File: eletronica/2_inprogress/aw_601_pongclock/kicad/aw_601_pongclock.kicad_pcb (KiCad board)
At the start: 2 copper layers, 149.9 x 199.4 mm, 89 parts, among them IC1 ATMEGA8-P, Q1 2N3904G, Q10 2N3904G, Q11 2N3904G, Q12 2N3904G, Q13 2N3904G, Q14 2N3904G, Q15 2N3904G, Q16 2N3904G, Q17 2N3904G, Q18 2N3904G, Q19 2N3904G, Q2 2N3904G, Q20 2N3904G, Q21 2N3904G, Q22 2N3904G, Q23 2N3904G, Q24 2N3904G, Q25 2N3904G, Q26 2N3904G, Q27 2N3904G, Q28 2N3904G, Q29 2N3904G, Q3 2N3904G, Q30 2N3904G, Q31 2N3904G, Q32 2N3904G, Q4 2N3904G, Q5 2N3904G, Q6 2N3904G, Q7 2N3904G, Q8 2N3904G, Q9 2N3904G, SW1 SW_PUSH, SW2 SW_PUSH, SW3 SW_PUSH, SW4 SW_PUSH, U1 4514, U2 ULN2803, U3 ULN2803, U4 ULN2803, U5 ULN2803, U6 74HC4094, U7 74HC4094, U8 74HC4094, U9 74HC4094, X1 16Mhz

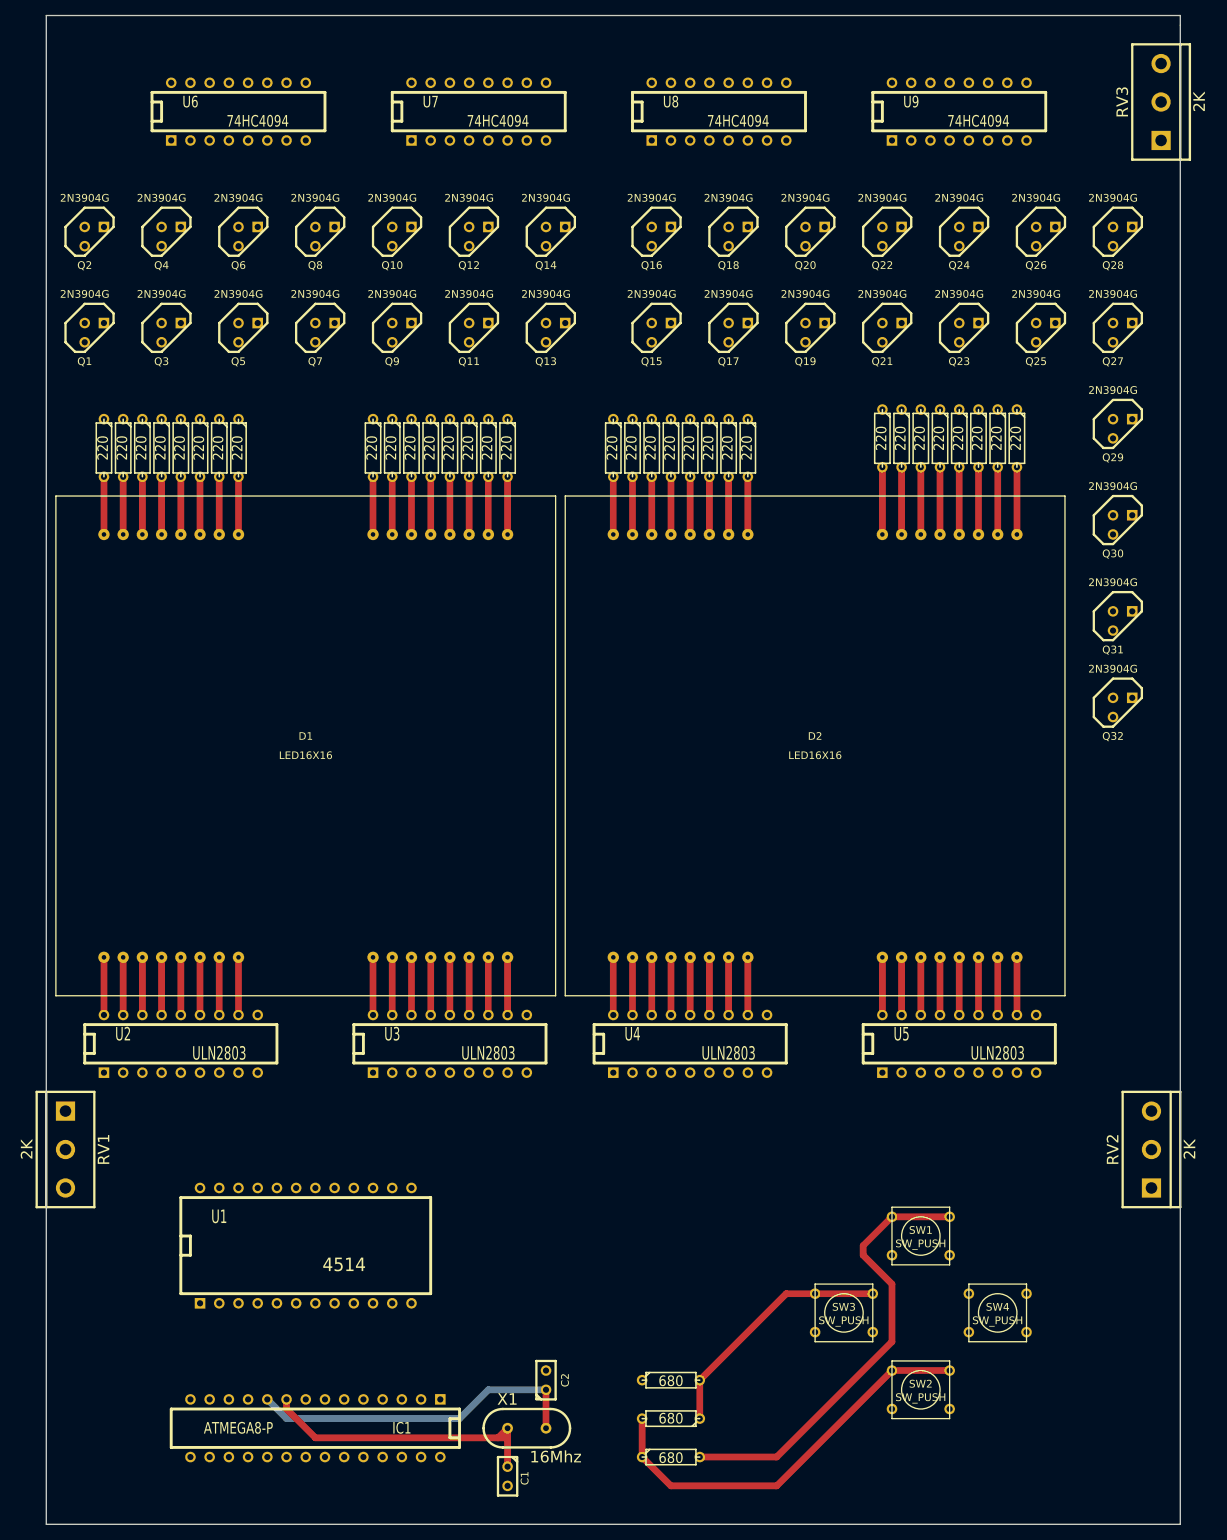
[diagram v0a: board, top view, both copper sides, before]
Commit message: 
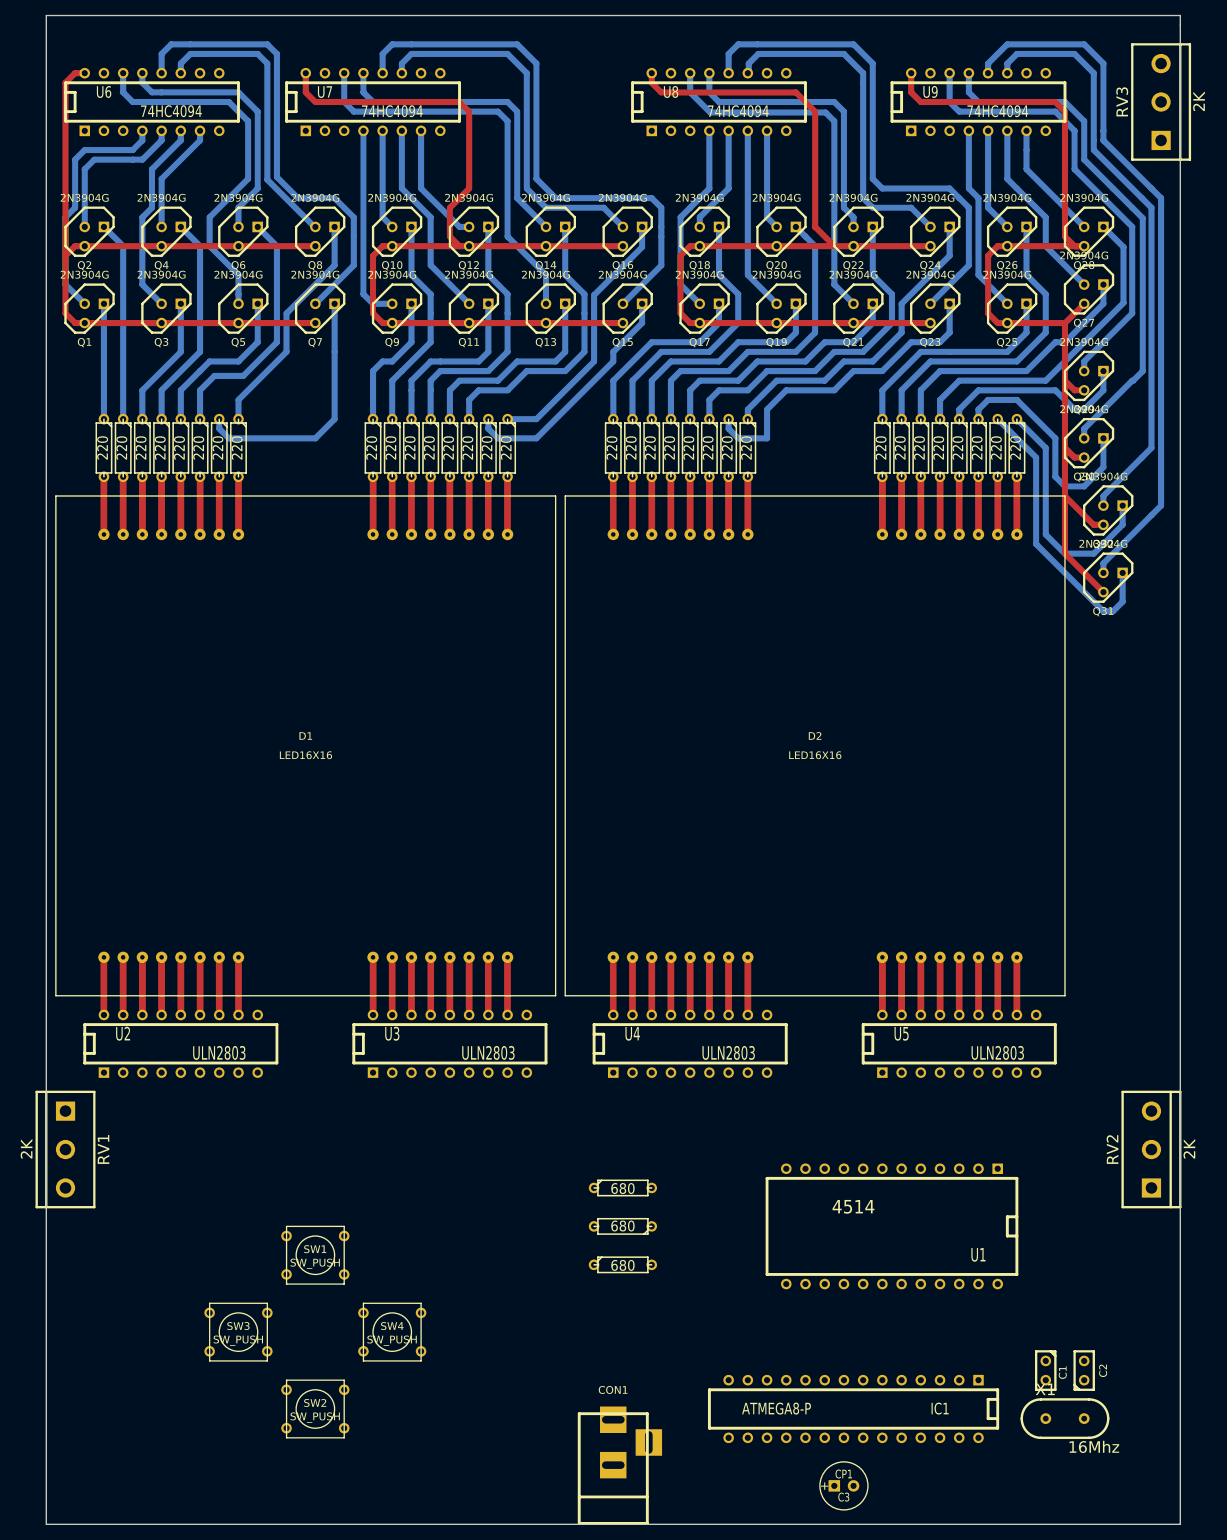
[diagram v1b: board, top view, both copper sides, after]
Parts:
- added C3: CP1, C1V7, F.Cu at (141.0, 232.4)
- added CON1: BARREL_JACK, BARREL_JACK, F.Cu at (110.5, 229.9)
- moved SW1 80.1 mm to (71.1, 201.9)
- moved SW2 80.1 mm to (71.1, 222.2)
- moved SW3 80.1 mm to (61.0, 212.1)
- moved SW4 80.1 mm to (81.3, 212.1)
- moved U1 77.5 mm to (147.3, 198.1), turned to 180 degrees
- moved C1 72.5 mm to (167.6, 217.2)
- moved IC1 71.2 mm to (142.2, 222.2)
- moved C2 71.1 mm to (172.7, 217.2)
- moved X1 71.1 mm to (170.2, 223.5)
- moved R1 26.2 mm to (111.8, 203.2)
- moved R2 26.2 mm to (111.8, 198.1)
- moved R3 26.2 mm to (111.8, 193.0)
- moved Q32 25.4 mm to (176.5, 104.1)
- moved U7 14.0 mm to (78.7, 49.5)
- moved U6 11.5 mm to (49.5, 49.5)
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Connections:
- Q1 pad 1: (no net) -> N-000008
- Q1 pad 2: N-0000027 -> /V1
- Q10 pad 1: (no net) -> N-000004
- Q10 pad 2: N-0000045 (its old number) -> /V10
- Q11 pad 1: (no net) -> N-000005
- Q11 pad 2: N-0000049 -> /V11
- Q12 pad 1: (no net) -> N-000006
- Q12 pad 2: N-0000050 -> /V12
- Q13 pad 1: (no net) -> N-0000019
- Q14 pad 1: (no net) -> N-0000020
- Q15 pad 1: (no net) -> N-0000021
- Q16 pad 1: (no net) -> N-0000022
- Q17 pad 1: (no net) -> N-0000016
- Q18 pad 1: (no net) -> N-0000015
- Q19 pad 1: (no net) -> N-0000014
- Q2 pad 1: (no net) -> N-0000012
- Q2 pad 2: N-0000054 -> /V2
- Q20 pad 1: (no net) -> N-0000013
- Q21 pad 1: (no net) -> N-0000024
- Q22 pad 1: (no net) -> N-0000023
- Q23 pad 1: (no net) -> N-0000017
- Q24 pad 1: (no net) -> N-0000018
- Q25 pad 1: (no net) -> N-0000064
- Q26 pad 1: (no net) -> N-0000065
- Q27 pad 1: (no net) -> N-0000066
- Q28 pad 1: (no net) -> N-0000067
- Q29 pad 1: (no net) -> N-0000068
- Q3 pad 1: (no net) -> N-000007
- Q3 pad 2: N-0000053 -> /V3
- Q30 pad 1: (no net) -> N-0000060
- Q31 pad 1: (no net) -> N-0000061
- Q32 pad 1: (no net) -> N-0000062
- Q4 pad 1: (no net) -> N-0000011
- Q4 pad 2: N-0000052 -> /V4
- Q5 pad 1: (no net) -> N-0000010
- Q5 pad 2: N-0000051 -> /V5
- Q6 pad 1: (no net) -> N-000009
- Q7 pad 1: (no net) -> N-000001
- Q7 pad 2: N-0000046 (its old number) -> /V7
- Q8 pad 1: (no net) -> N-000002
- Q8 pad 2: N-0000047 -> /V8
- Q9 pad 1: (no net) -> N-000003
- Q9 pad 2: N-0000048 -> /V9
- R10 pad 1: N-0000046 (its old number) -> N-000001
- R27 pad 1: N-0000047 -> N-000002
- R28 pad 1: N-0000048 -> N-000003
- R29 pad 1: N-0000045 (its old number) -> N-000004
- R30 pad 1: N-0000049 -> N-000005
- R31 pad 1: N-0000050 -> N-000006
- R32 pad 1: (no net) -> N-0000019
- R33 pad 1: (no net) -> N-0000020
- R34 pad 1: (no net) -> N-0000021
- R35 pad 1: (no net) -> N-0000022
- R4 pad 1: N-0000027 -> N-000008
- R5 pad 1: N-0000054 -> N-0000012
- R52 pad 1: (no net) -> N-0000016
- R53 pad 1: (no net) -> N-0000015
- R54 pad 1: (no net) -> N-0000014
- R55 pad 1: (no net) -> N-0000013
- R56 pad 1: (no net) -> N-0000024
- R57 pad 1: (no net) -> N-0000023
- R58 pad 1: (no net) -> N-0000017
- R59 pad 1: (no net) -> N-0000018
- R6 pad 1: N-0000053 -> N-000007
- R60 pad 1: (no net) -> N-0000064
- R61 pad 1: (no net) -> N-0000065
- R62 pad 1: (no net) -> N-0000066
- R63 pad 1: (no net) -> N-0000067
- R64 pad 1: (no net) -> N-0000068
- R65 pad 1: (no net) -> N-0000060
- R66 pad 1: (no net) -> N-0000061
- R67 pad 1: (no net) -> N-0000062
- R7 pad 1: N-0000052 -> N-0000011
- R8 pad 1: N-0000051 -> N-0000010
- R9 pad 1: (no net) -> N-000009
- U6 pad 11: (no net) -> /V8
- U6 pad 12: (no net) -> /V7
- U6 pad 14: (no net) -> /V5
- U6 pad 4: (no net) -> /V1
- U6 pad 5: (no net) -> /V2
- U6 pad 6: (no net) -> /V3
- U6 pad 7: (no net) -> /V4
- U7 pad 4: (no net) -> /V9
- U7 pad 5: (no net) -> /V10
- U7 pad 6: (no net) -> /V11
- U7 pad 7: (no net) -> /V12
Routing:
- net +5V: track 0.00 -> 466.9 mm
- net /V31: track 0.00 -> 92.2 mm
- net /V32: track 0.00 -> 77.2 mm
- net /V15: track 0.00 -> 72.6 mm
- net /V30: track 0.00 -> 67.8 mm
- net /V23: track 0.00 -> 67.5 mm
- net /V7: track 0.00 -> 61.0 mm
- net /V29: track 0.00 -> 59.4 mm
- net N-00000105: track 59.0 -> 0.00 mm
- net N-00000103: track 53.6 -> 0.00 mm
- net /V13: track 0.00 -> 52.7 mm
- net /V16: track 0.00 -> 49.4 mm
- net /V5: track 0.00 -> 48.4 mm
- net /V21: track 0.00 -> 48.4 mm
- net /V24: track 0.00 -> 45.0 mm
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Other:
- net class Default: clearance 0.5 -> 0.35; trace_width 0.889 -> 0.8
- rule trace_clearance: 0.5 -> 0.35

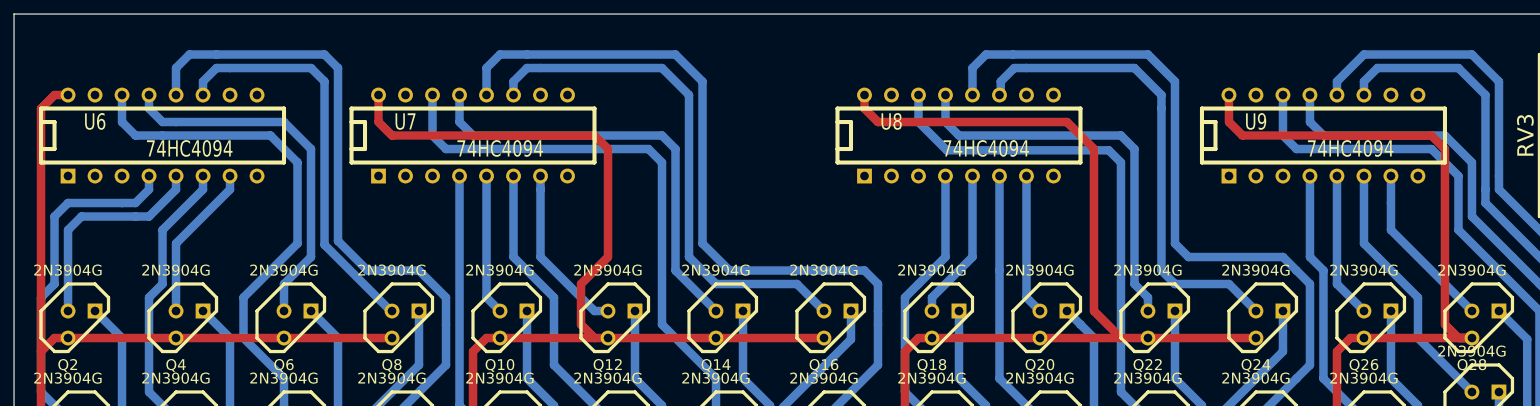
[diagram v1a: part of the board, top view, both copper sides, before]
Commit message: 
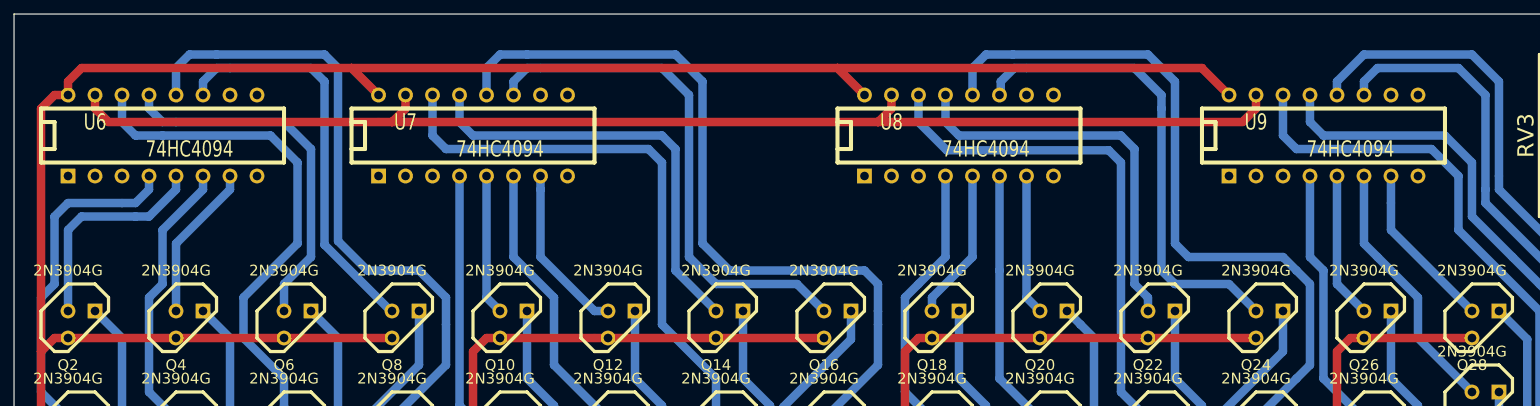
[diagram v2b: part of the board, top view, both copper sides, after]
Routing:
- net /OE: track 0.00 -> 118.9 mm
- net +5V: track 466.9 -> 454.9 mm
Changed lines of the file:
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@@
   (general
     (links 273)
-    (no_connects 113)
+    (no_connects 110)
     (area 31.7556 38.049999 189.2244 237.911121)
     (thickness 1.6)
     (drawings 5)
-    (tracks 588)
+    (tracks 587)
     (zones 0)
     (modules 91)
@@
   (gr_line (start 35.56 237.49) (end 185.42 237.49) (angle 90) (layer Edge.Cuts) (width 0.1))
   (gr_line (start 35.56 38.1) (end 35.56 237.49) (angle 90) (layer Edge.Cuts) (width 0.1))
-  (segment (start 149.86 45.72) (end 149.86 48.26) (width 0.8) (layer F.Cu) (net 1) (status 400000))
-  (segment (start 171.45 68.58) (end 172.72 68.58) (width 0.8) (layer F.Cu) (net 1) (status 800000))
-  (segment (start 170.18 67.31) (end 171.45 68.58) (width 0.8) (layer F.Cu) (net 1))
-  (segment (start 170.18 50.8) (end 170.18 67.31) (width 0.8) (layer F.Cu) (net 1))
-  (segment (start 168.91 49.53) (end 170.18 50.8) (width 0.8) (layer F.Cu) (net 1))
-  (segment (start 151.13 49.53) (end 168.91 49.53) (width 0.8) (layer F.Cu) (net 1))
-  (segment (start 149.86 48.26) (end 151.13 49.53) (width 0.8) (layer F.Cu) (net 1))
-  (segment (start 115.57 45.72) (end 115.57 46.99) (width 0.8) (layer F.Cu) (net 1) (status 400000))
-  (segment (start 137.16 66.04) (end 139.7 68.58) (width 0.8) (layer F.Cu) (net 1))
-  (segment (start 137.16 50.8) (end 137.16 66.04) (width 0.8) (layer F.Cu) (net 1))
-  (segment (start 134.62 48.26) (end 137.16 50.8) (width 0.8) (layer F.Cu) (net 1))
-  (segment (start 116.84 48.26) (end 134.62 48.26) (width 0.8) (layer F.Cu) (net 1))
-  (segment (start 115.57 46.99) (end 116.84 48.26) (width 0.8) (layer F.Cu) (net 1))
-  (segment (start 91.44 60.96) (end 91.44 50.8) (width 0.8) (layer F.Cu) (net 1))
-  (segment (start 69.85 48.26) (end 71.12 49.53) (width 0.8) (layer F.Cu) (net 1))
-  (segment (start 71.12 49.53) (end 90.17 49.53) (width 0.8) (layer F.Cu) (net 1))
-  (segment (start 90.17 49.53) (end 91.44 50.8) (width 0.8) (layer F.Cu) (net 1))
-  (segment (start 91.44 60.96) (end 88.9 63.5) (width 0.8) (layer F.Cu) (net 1))
-  (segment (start 88.9 63.5) (end 88.9 67.31) (width 0.8) (layer F.Cu) (net 1))
-  (segment (start 90.17 68.58) (end 88.9 67.31) (width 0.8) (layer F.Cu) (net 1))
-  (segment (start 69.85 48.26) (end 69.85 45.72) (width 0.8) (layer F.Cu) (net 1) (status 800000))
+  (segment (start 113.03 43.18) (end 147.32 43.18) (width 0.8) (layer F.Cu) (net 1))
+  (segment (start 147.32 43.18) (end 149.86 45.72) (width 0.8) (layer F.Cu) (net 1) (status 800000))
+  (segment (start 67.31 43.18) (end 113.03 43.18) (width 0.8) (layer F.Cu) (net 1))
+  (segment (start 113.03 43.18) (end 115.57 45.72) (width 0.8) (layer F.Cu) (net 1) (status 800000))
+  (segment (start 40.64 45.72) (end 40.64 44.45) (width 0.8) (layer F.Cu) (net 1) (status 400000))
+  (segment (start 67.31 43.18) (end 69.85 45.72) (width 0.8) (layer F.Cu) (net 1) (status 800000))
+  (segment (start 41.91 43.18) (end 67.31 43.18) (width 0.8) (layer F.Cu) (net 1))
+  (segment (start 40.64 44.45) (end 41.91 43.18) (width 0.8) (layer F.Cu) (net 1))
   (segment (start 40.64 45.72) (end 39.37 45.72) (width 0.8) (layer F.Cu) (net 1) (status 400000))
   (segment (start 38.1 46.99) (end 38.1 69.85) (width 0.8) (layer F.Cu) (net 1))
@@
   (segment (start 60.96 162.56) (end 60.96 170.18) (width 0.889) (layer F.Cu) (net 41))
   (segment (start 78.74 162.56) (end 78.74 170.18) (width 0.889) (layer F.Cu) (net 42))
+  (segment (start 71.12 48.26) (end 72.39 46.99) (width 0.8) (layer F.Cu) (net 43))
+  (segment (start 72.39 46.99) (end 72.39 45.72) (width 0.8) (layer F.Cu) (net 43) (status 800000))
+  (segment (start 116.84 48.26) (end 151.13 48.26) (width 0.8) (layer F.Cu) (net 43))
+  (segment (start 152.4 46.99) (end 152.4 45.72) (width 0.8) (layer F.Cu) (net 43) (status 800000))
+  (segment (start 151.13 48.26) (end 152.4 46.99) (width 0.8) (layer F.Cu) (net 43))
+  (segment (start 69.85 48.26) (end 71.12 48.26) (width 0.8) (layer F.Cu) (net 43))
+  (segment (start 71.12 48.26) (end 116.84 48.26) (width 0.8) (layer F.Cu) (net 43))
+  (segment (start 118.11 46.99) (end 118.11 45.72) (width 0.8) (layer F.Cu) (net 43) (status 800000))
+  (segment (start 116.84 48.26) (end 118.11 46.99) (width 0.8) (layer F.Cu) (net 43))
+  (segment (start 43.18 45.72) (end 43.18 46.99) (width 0.8) (layer F.Cu) (net 43) (status 400000))
+  (segment (start 44.45 48.26) (end 69.85 48.26) (width 0.8) (layer F.Cu) (net 43))
+  (segment (start 43.18 46.99) (end 44.45 48.26) (width 0.8) (layer F.Cu) (net 43))
   (segment (start 38.1 73.66) (end 38.1 64.77) (width 0.8) (layer B.Cu) (net 46))
   (segment (start 40.64 55.88) (end 45.72 55.88) (width 0.8) (layer B.Cu) (net 46))
